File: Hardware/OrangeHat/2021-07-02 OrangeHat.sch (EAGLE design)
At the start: 28 parts, among them CON485A JACK_SMD_3MM5, CON485B JACK_SMD_3MM5, IC485 SN75176

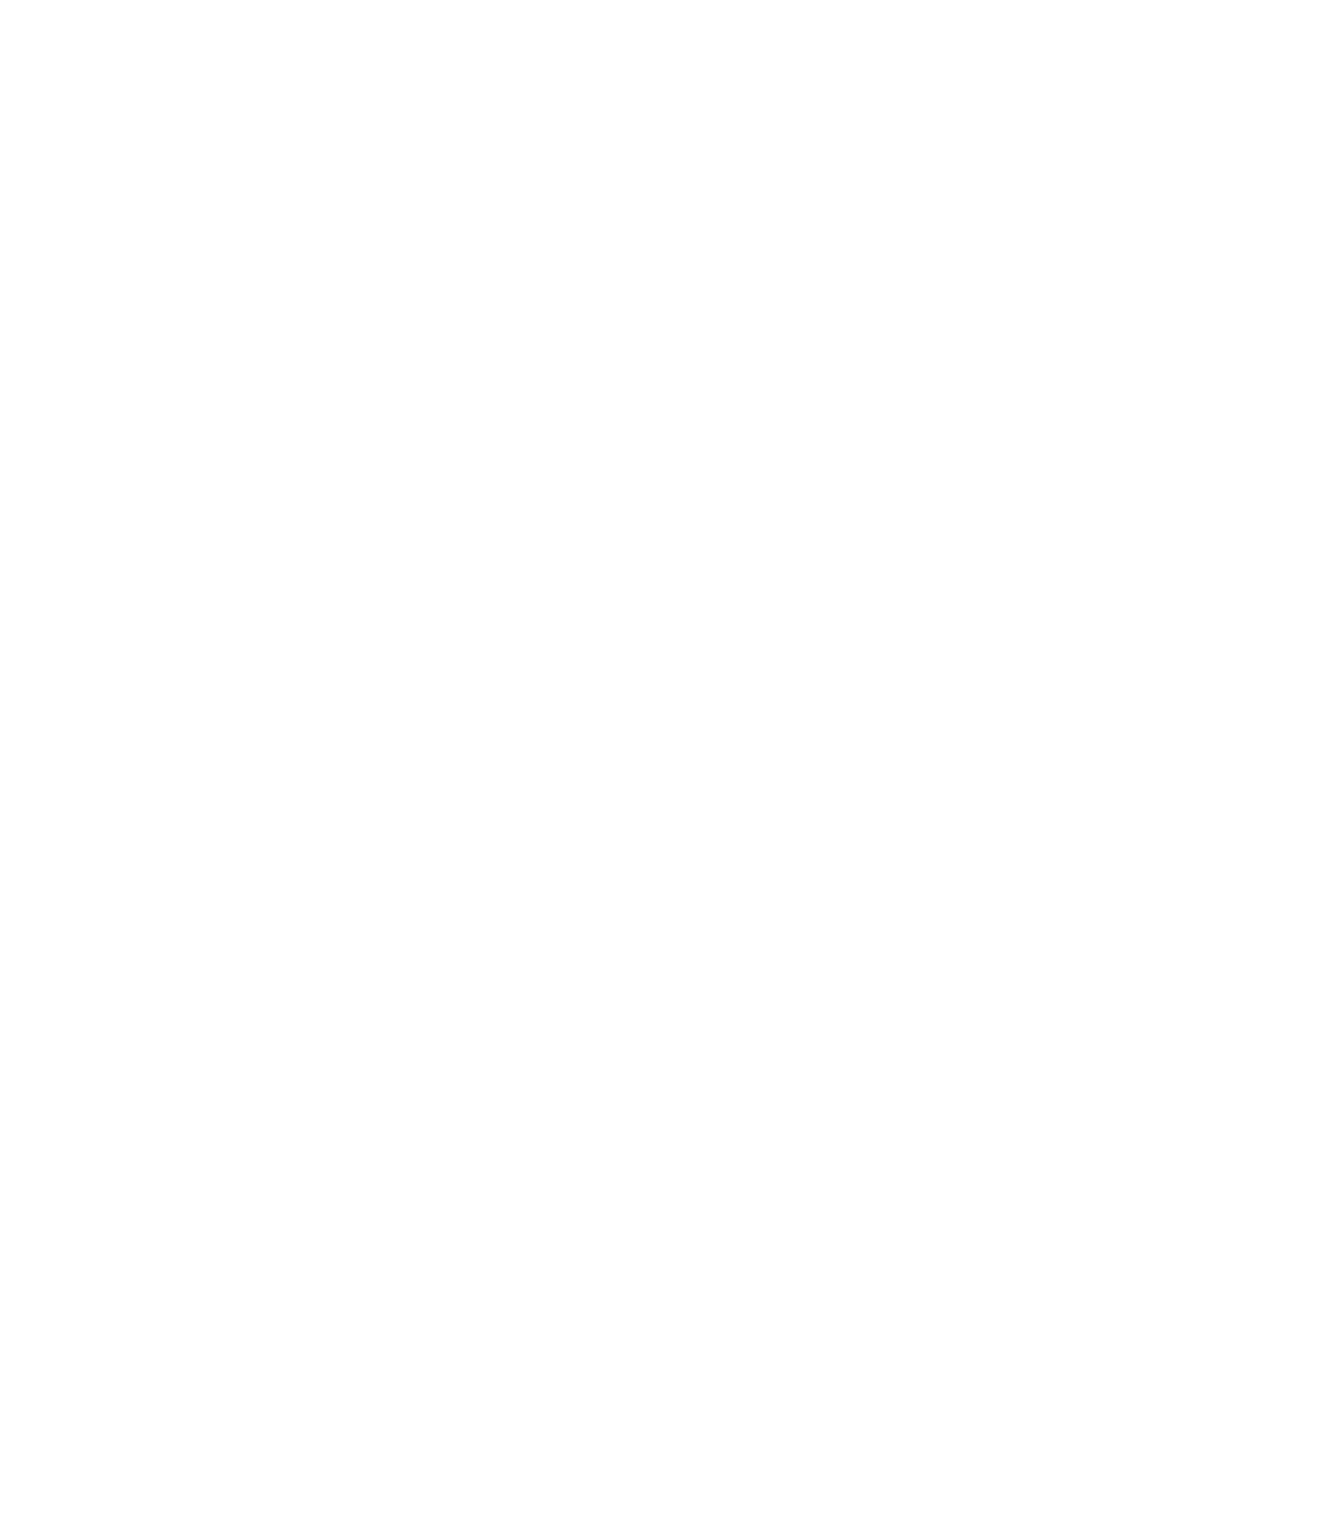
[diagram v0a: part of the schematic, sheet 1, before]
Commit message: Add files via upload
LCD Display Schematics and Initial Placement
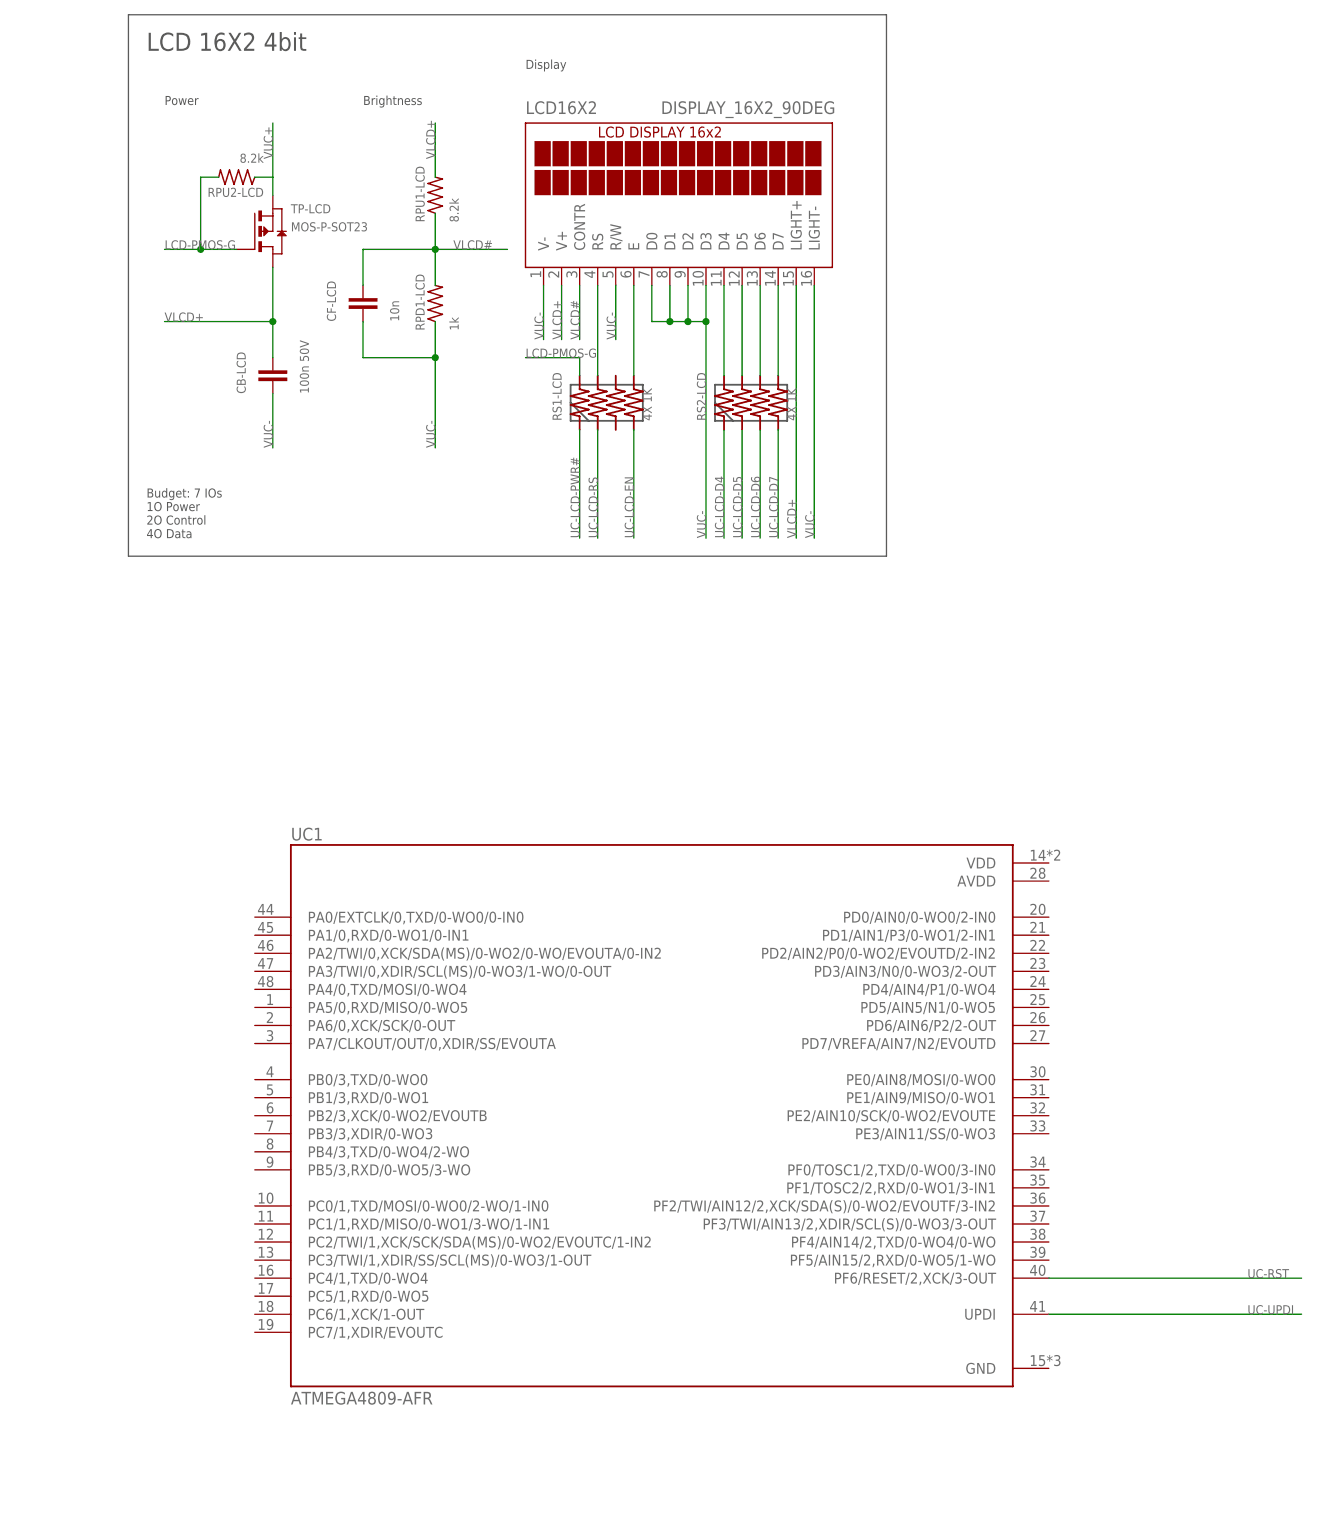
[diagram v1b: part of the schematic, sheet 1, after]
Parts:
- removed DIS1: DISPLAY_16X2_90DEG, 2021-07-02 OrangeHat Library:DISPLAY_16X2_90DEG
- added CB-LCD: 100n 50V, 2021-07-02 OrangeHat Library:C-NPOLC0805
- added CF-LCD: 10n, 2021-07-02 OrangeHat Library:C-NPOLC0805
- added LCD16X2: DISPLAY_16X2_90DEG, 2021-07-02 OrangeHat Library:DISPLAY_16X2_90DEG
- added RPD1-LCD: 1k, 2021-07-02 OrangeHat Library:RM0805
- added RPU1-LCD, RPU2-LCD: 8.2k, 2021-07-02 OrangeHat Library:RM0805
- added RS1-LCD, RS2-LCD: 4X 1K, 2021-07-02 OrangeHat Library:RAC164
- added TP-LCD: MOS-P-SOT23, 2021-07-02 OrangeHat Library:MOS-P-SOT23
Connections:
- removed net N$14: DIS1.LIGHT+
- removed net N$15: DIS1.LIGHT-
- removed net N$3: DIS1.V-
- removed net N$5: DIS1.V+
- removed net N$6: DIS1.CONTR
- removed net N$8: DIS1.R/W
- new net LCD-PMOS-G: RPU2-LCD.2, RS1-LCD.1B, TP-LCD.G
- new net UC-LCD-D4: RS2-LCD.1A
- new net UC-LCD-D5: RS2-LCD.2A
- new net UC-LCD-D6: RS2-LCD.3A
- new net UC-LCD-D7: RS2-LCD.4A
- new net UC-LCD-EN: RS1-LCD.4A
- new net UC-LCD-PWR#: RS1-LCD.1A
- new net UC-LCD-RS: RS1-LCD.2A
- new net VLCD#: CF-LCD.2, LCD16X2.CONTR, RPD1-LCD.2, RPU1-LCD.1
- new net VLCD+: CB-LCD.2, LCD16X2.LIGHT+, LCD16X2.V+, RPU1-LCD.2, TP-LCD.D
- net N$10: now also LCD16X2.D4, RS2-LCD.1B; no longer DIS1.D4
- net N$11: now also LCD16X2.D5, RS2-LCD.2B; no longer DIS1.D5
- net N$12: now also LCD16X2.D6, RS2-LCD.3B; no longer DIS1.D6
- net N$13: now also LCD16X2.D7, RS2-LCD.4B; no longer DIS1.D7
- net N$7: now also LCD16X2.RS, RS1-LCD.2B; no longer DIS1.RS
- net N$9: now also LCD16X2.E, RS1-LCD.4B; no longer DIS1.E
- net VUC+: now also RPU2-LCD.1, TP-LCD.S
- net VUC-: now also CB-LCD.1, CF-LCD.1, LCD16X2.D0, LCD16X2.D1, LCD16X2.D2, LCD16X2.D3, LCD16X2.LIGHT-, LCD16X2.R/W, LCD16X2.V-, RPD1-LCD.1
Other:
- note added: "Brightness"
- note added: "Budget: 7 IOs 1O Power 2O Control 4O Data"
- note added: "Display"
- note added: "LCD 16X2 4bit"
- note added: "Power"

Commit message: Add files via upload
Added Servo schematics and initial placement. Adjusted/created footprints.
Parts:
- removed U$10, U$11, U$4, U$5, U$6, U$7, U$8, U$9: PIWARSRPIHAT_CON3254-MIN, 2021-07-02 OrangeHat Library:PIWARSRPIHAT_CON3254-MIN
- added CB1-SRVO, CB1-SRVO1, CB2-SRVO, CB3-SRVO: 1u, 2021-07-02 OrangeHat Library:C-NPOLC0805
- added CF2-SRVO: 10n, 2021-07-02 OrangeHat Library:C-NPOLC0805
- added CP-SRVO: 100uF 6V3, 2021-07-02 OrangeHat Library:C-POLE2.5-5
- added F-SRVO: PTC-M5040, 2021-07-02 OrangeHat Library:PTC-M5040
- added LF1-SRVO, LF1-SRVO1: BEAD 3A, 2021-07-02 OrangeHat Library:L-M2016
- added RD2-SRVO: 1k, 2021-07-02 OrangeHat Library:RM0805
- added RS1-SRVO, RS2-SRVO: 4X 1K, 2021-07-02 OrangeHat Library:RAC164
- added RS3-SRVO: 1K, 2021-07-02 OrangeHat Library:RM0805
- added RU1-SRVO: 100k, 2021-07-02 OrangeHat Library:RM0805
- added RU2-SRVO: 8.2k, 2021-07-02 OrangeHat Library:RM0805
- added TP-SRVO: MOS-P-TO252, 2021-07-02 OrangeHat Library:MOS-P-TO252
- added U$1: SERVO8, 2021-07-02 OrangeHat Library:SERVO8
- added U$3: ACS712, 2021-07-02 OrangeHat Library:ACS712
- renumbered RPD1-LCD to RD1-LCD, RPU1-LCD to RU1-LCD, RPU2-LCD to RU2-LCD
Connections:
- new net N$15: CB1-SRVO.1, LF1-SRVO1.1
- new net N$21: CB1-SRVO1.2, U$3.FILTER
- new net N$23: RS2-SRVO.1A, U$1.8
- new net N$24: RS2-SRVO.2A, U$1.7
- new net N$25: RS2-SRVO.3A, U$1.6
- new net N$26: RS2-SRVO.4A, U$1.5
- new net N$27: RS1-SRVO.1A, U$1.4
- new net N$28: RS1-SRVO.2A, U$1.3
- new net N$29: RS1-SRVO.3A, U$1.2
- new net N$3: F-SRVO.1
- new net N$30: RS1-SRVO.4A, U$1.1
- new net N$5: RS3-SRVO.2, RU1-SRVO.2, TP-SRVO.G
- new net N$6: F-SRVO.2, RU1-SRVO.1, TP-SRVO.S
- new net UC-ISRVO: U$3.SENSE
- new net UC-SRVO-PWR#: RS3-SRVO.1
- new net UC-SRVO1: RS1-SRVO.4B
- new net UC-SRVO2: RS1-SRVO.3B
- new net UC-SRVO3: RS1-SRVO.2B
- new net UC-SRVO4: RS1-SRVO.1B
- new net UC-SRVO5: RS2-SRVO.4B
- new net UC-SRVO6: RS2-SRVO.3B
- new net UC-SRVO7: RS2-SRVO.2B
- new net UC-SRVO8: RS2-SRVO.1B
- new net UC-VSRVO: CF2-SRVO.2, RD2-SRVO.2, RU2-SRVO.1
- new net VSRVO#A: RU2-SRVO.2, TP-SRVO.D, U$3.IIN
- new net VSRVO#B: CB1-SRVO.2, LF1-SRVO.1, U$3.IOUT
- new net VSRVO+: CB2-SRVO.2, CB3-SRVO.2, CP-SRVO.+, LF1-SRVO.2, U$1.+
- new net VSRVO-: CB2-SRVO.1, CB3-SRVO.1, CP-SRVO.-, LF1-SRVO1.2, U$1.-
- net VUC+: now also U$3.+
- net VUC-: now also CB1-SRVO1.1, CF2-SRVO.1, RD2-SRVO.1, U$3.-
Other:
- note added: "BUDGET: 11 IOs 1O Power 8O PPM 50Hz 2I ADC"
- note added: "BUDGET: 3 IOs 1O Control 2X UART"
- note added: "BUDGET: 7 IOs 1O Power 2O Control 4O Data"
- note added: "Current Sense"
- note added: "Filters"
- note added: "IDEAS: UC+PMOS power control"
- note added: "Power Switch"
- note added: "SERVO"
- note added: "Servo Connectors"
- note added: "Voltage Sense"
- note removed: "Budget: 7 IOs 1O Power 2O Control 4O Data"
- moved on the sheet: LCD16X2, RS1-LCD, RS2-LCD

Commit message: Add files via upload
Adds LED for servo power
Tidy up packages and keepouts
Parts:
- removed CB485: 100n 50V, 2021-07-02 OrangeHat Library:C-NPOLC0805
- removed CF485: 100n 50v, 2021-07-02 OrangeHat Library:C-NPOLC0805
- removed CON485A, CON485B: JACK_SMD_3MM5, 2021-07-02 OrangeHat Library:JACK_SMD_3MM5
- removed CP485: 100uF 6V3, 2021-07-02 OrangeHat Library:C-POLE2.5-5
- removed IC485: SN75176, 2021-07-02 OrangeHat Library:RS485
- removed LF485A, LF485B: BEAD 500mA, 2021-07-02 OrangeHat Library:L-0805
- removed RPD485, RPU485: 720, 2021-07-02 OrangeHat Library:RM0805
- removed RS458A: 4X 1K, 2021-07-02 OrangeHat Library:RAC164
- removed RS485B, RS485C: 10, 2021-07-02 OrangeHat Library:RR0805
- removed RT485: 120, 2021-07-02 OrangeHat Library:RM0805
- added CB-485: 100n 50V, 2021-07-02 OrangeHat Library:C-NPOL
- added CF-485: 100n 50v, 2021-07-02 OrangeHat Library:C-NPOL
- added CON1-485, CON2-485: JACK_SMD_3MM5, 2021-07-02 OrangeHat Library:JACK_SMD_3MM5
- added CP-485: 100uF 6V3, 2021-07-02 OrangeHat Library:C-POLE2.5-5
- added DL-SRVO: LED, 2021-07-02 OrangeHat Library:LED
- added IC-485: SN75176, 2021-07-02 OrangeHat Library:RS485
- added LF1-485, LF2-485: BEAD 500mA, 2021-07-02 OrangeHat Library:L-M2012
- added RD-485, RU-485: 720, 2021-07-02 OrangeHat Library:R-M2012
- added RD-SRVO: 1K, 2021-07-02 OrangeHat Library:R-M2012
- added RS1-458: 4X 1K, 2021-07-02 OrangeHat Library:RAC164
- added RS2-485, RS3-485: 10, 2021-07-02 OrangeHat Library:R-M2012
- added RT-485: 120, 2021-07-02 OrangeHat Library:R-M2012
- CB-LCD, CB1-SRVO, CB1-SRVO1, CB2-SRVO, CB3-SRVO, CF-LCD, CF2-SRVO: device 2021-07-02 OrangeHat Library:C-NPOLC0805 -> 2021-07-02 OrangeHat Library:C-NPOL
- RD1-LCD, RD2-SRVO, RS3-SRVO, RU1-LCD, RU1-SRVO, RU2-LCD, RU2-SRVO: device 2021-07-02 OrangeHat Library:RM0805 -> 2021-07-02 OrangeHat Library:R-M2012
- renumbered U$3 to IC-SRVO
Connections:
- new net N$22: DL-SRVO.+, RD-SRVO.2
- net CHA485: now also CON1-485.L, CON1-485.LX, CON2-485.L, CON2-485.LX, IC-485.A, RD-485.2, RT-485.1; no longer CON485A.L, CON485A.LX, CON485B.L, CON485B.LX, IC485.A, RPD485.2, RT485.1
- net CHB485: now also CON1-485.R, CON1-485.RX, CON2-485.R, CON2-485.RX, IC-485.B, RT-485.2, RU-485.1; no longer CON485A.R, CON485A.RX, CON485B.R, CON485B.RX, IC485.B, RPU485.1, RT485.2
- net N$1: now also IC-485.RXO, RS1-458.1B; no longer IC485.RXO, RS458A.1B
- net N$16: now also IC-485.TXI, RS1-458.4B; no longer IC485.TXI, RS458A.4B
- net N$17: now also CON1-485.SHIELD, RS2-485.2; no longer CON485A.SHIELD, RS485B.2
- net N$18: now also CON2-485.SHIELD, RS3-485.2; no longer CON485B.SHIELD, RS485C.2
- net N$19: now also CF-485.1, LF2-485.1; no longer CF485.1, LF485B.1
- net N$2: now also IC-485.RXEN#, RS1-458.2B; no longer IC485.RXEN#, RS458A.2B
- net N$20: now also CF-485.2, LF1-485.1; no longer CF485.2, LF485A.1
- net N$4: now also IC-485.TXEN, RS1-458.3B; no longer IC485.TXEN, RS458A.3B
- net UC_RXI485: now also RS1-458.1A; no longer RS458A.1A
- net UC_TXEN485: now also RS1-458.3A; no longer RS458A.3A
- net UC_TXO485: now also RS1-458.4A; no longer RS458A.4A
- net V+485: now also CB-485.2, CP-485.+, IC-485.V+, LF1-485.2, RU-485.2; no longer CB485.2, CP485.+, IC485.V+, LF485A.2, RPU485.2
- net V-485: now also CB-485.1, CP-485.-, IC-485.V-, LF2-485.2, RD-485.1, RS1-458.2A, RS2-485.1, RS3-485.1; no longer CB485.1, CP485.-, IC485.V-, LF485B.2, RPD485.1, RS458A.2A, RS485B.1, RS485C.1
- net VSRVO+: now also RD-SRVO.1
- net VSRVO-: now also DL-SRVO.-
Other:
- note added: "LED"

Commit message: Assigns microcontroller pins. Draws power planes.
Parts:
- removed CB-485: 100n 50V, 2021-07-02 OrangeHat Library:C-NPOL
- removed CF-485: 100n 50v, 2021-07-02 OrangeHat Library:C-NPOL
- removed CON1-485, CON2-485: JACK_SMD_3MM5, 2021-07-02 OrangeHat Library:JACK_SMD_3MM5
- removed CP-485: 100uF 6V3, 2021-07-02 OrangeHat Library:C-POLE2.5-5
- removed IC-485: SN75176, 2021-07-02 OrangeHat Library:RS485
- removed LF1-485, LF2-485: BEAD 500mA, 2021-07-02 OrangeHat Library:L-M2012
- removed RS1-458: 4X 1K, 2021-07-02 OrangeHat Library:RAC164
- removed U$2: 2020-03-18-BUCK, 2021-07-02 OrangeHat Library:2020-03-18-BUCK
- removed UC1: ATMEGA4809-AFR, 2021-07-02 OrangeHat Library:ATMEGA4809-AFR
- added CB-UC-1, CB-UC-2, CB-UC-3, CB-UC-4, CB1-485: 100n 50V, 2021-07-02 OrangeHat Library:C-NPOL
- added CF1-485: 100n 50v, 2021-07-02 OrangeHat Library:C-NPOL
- added CON1-1, CON2-1: JACK_SMD_3MM5, 2021-07-02 OrangeHat Library:JACK_SMD_3MM5
- added CP1-485: 100uF 6V3, 2021-07-02 OrangeHat Library:C-POLE2.5-5
- added IC-UC-1: ATMEGA4809-AFR, 2021-07-02 OrangeHat Library:ATMEGA4809-AFR
- added IC1-485: SN75176, 2021-07-02 OrangeHat Library:RS485
- added LF-UC-1, LF1-1, LF2-1: BEAD 500mA, 2021-07-02 OrangeHat Library:L-M2012
- added MOD-BUCK: 2020-03-18-BUCK, 2021-07-02 OrangeHat Library:2020-03-18-BUCK
- added RD-UC-1, RU-UC-1: 100k, 2021-07-02 OrangeHat Library:R-M2012
- added RS-RPI-1, RS1-485: 4X 1K, 2021-07-02 OrangeHat Library:RAC164
- added TN-UC-1: MOS-N-SOT23, 2021-07-02 OrangeHat Library:MOS-N-SOT23
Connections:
- removed net IMU-SCL: IMU1.I2C-SDL
- removed net IMU-SDA: IMU1.I2C-SDA
- removed net N$1: IC-485.RXO, RS1-458.1B
- removed net N$16: IC-485.TXI, RS1-458.4B
- removed net N$18: CON2-485.SHIELD, RS3-485.2
- removed net N$2: IC-485.RXEN#, RS1-458.2B
- removed net N$4: IC-485.TXEN, RS1-458.3B
- removed net RPI-COM: CON-RPI.GND_1, CON-RPI.GND_2
- removed net RPI-VCC: CON-RPI.5V_1, CON-RPI.5V_2
- removed net UC_RXI485: RS1-458.1A
- removed net UC_TXEN485: RS1-458.3A
- removed net UC_TXO485: RS1-458.4A
- new net N$14: IC-UC-1.PF4/AIN14/2,TXD/0-WO4/0-WO
- new net N$42: IC-UC-1.PD6/AIN6/P2/2-OUT
- new net N$43: IC-UC-1.PD5/AIN5/N1/0-WO5
- new net N$44: IC1-485.TXEN, RS1-485.3B
- new net N$45: IC1-485.TXI, RS1-485.4B
- new net N$46: CON1-1.SHIELD, RS2-485.2
- new net N$47: CON2-1.SHIELD, RS3-485.2
- new net N$49: IC-UC-1.PC7/1,XDIR/EVOUTC
- new net N$50: IC-UC-1.PC6/1,XCK/1-OUT
- new net N$51: IC-UC-1.PC5/1,RXD/0-WO5
- new net N$52: IC-UC-1.PC4/1,TXD/0-WO4
- new net N$53: RS-RPI-1.4B
- new net N$62: IC-UC-1.PA6/0,XCK/SCK/0-OUT
- new net N$8: IC-UC-1.PF5/AIN15/2,RXD/0-WO5/1-WO
- new net UC-485-RXEN#: IC-UC-1.PC3/TWI/1,XDIR/SS/SCL(MS)/0-WO3/1-OUT, RS1-485.2A
- new net UC-485-RXI: IC-UC-1.PC1/1,RXD/MISO/0-WO1/3-WO/1-IN1, RS1-485.1A
- new net UC-485-TXEN: IC-UC-1.PC2/TWI/1,XCK/SCK/SDA(MS)/0-WO2/EVOUTC/1-IN2, RS1-485.3A
- new net UC-485-TXO: IC-UC-1.PC0/1,TXD/MOSI/0-WO0/2-WO/1-IN0, RS1-485.4A
- new net UC-IMU-FSYNC: IC-UC-1.PA5/0,RXD/MISO/0-WO5, IMU1.FSYNC
- new net UC-IMU-INT: IC-UC-1.PA4/0,TXD/MOSI/0-WO4, IMU1.INT
- new net UC-IMU-SCL: IC-UC-1.PA3/TWI/0,XDIR/SCL(MS)/0-WO3/1-WO/0-OUT, IMU1.I2C-SDL
- new net UC-IMU-SDA: IC-UC-1.PA2/TWI/0,XCK/SDA(MS)/0-WO2/0-WO/EVOUTA/0-IN2, IMU1.I2C-SDA
- new net UC-IRPI: IC-UC-1.PD2/AIN2/P0/0-WO2/EVOUTD/2-IN2
- new net UC-RPI-RXI: IC-UC-1.PA1/0,RXD/0-WO1/0-IN1, RS-RPI-1.2B
- new net UC-RPI-TXO: IC-UC-1.PA0/EXTCLK/0,TXD/0-WO0/0-IN0, RS-RPI-1.1B
- new net UC-RST#: IC-UC-1.PF6/RESET/2,XCK/3-OUT, RU-UC-1.1, TN-UC-1.D
- new net UC-VIN: IC-UC-1.PD0/AIN0/0-WO0/2-IN0
- new net UC-VRPI: IC-UC-1.PD1/AIN1/P3/0-WO1/2-IN1
- new net VADC+: CB-UC-4.2, IC-UC-1.AVDD, LF-UC-1.2
- new net VRPI+: CON-RPI.5V_1, CON-RPI.5V_2, MOD-BUCK.V5.2A3.0+
- new net VRPI-: CON-RPI.GND_1, CON-RPI.GND_2, MOD-BUCK.V5.2A3.0-
- net CHA485: now also CON1-1.L, CON1-1.LX, CON2-1.L, CON2-1.LX, IC1-485.A; no longer CON1-485.L, CON1-485.LX, CON2-485.L, CON2-485.LX, IC-485.A
- net CHB485: now also CON1-1.R, CON1-1.RX, CON2-1.R, CON2-1.RX, IC1-485.B; no longer CON1-485.R, CON1-485.RX, CON2-485.R, CON2-485.RX, IC-485.B
- net N$17: now also RS-RPI-1.4A; no longer CON1-485.SHIELD, RS2-485.2
- net N$19: now also CF1-485.1, IC1-485.RXO, LF2-1.1, RS1-485.1B; no longer CF-485.1, LF2-485.1
- net N$20: now also CF1-485.2, IC1-485.RXEN#, LF1-1.1, RS1-485.2B; no longer CF-485.2, LF1-485.1
- net RPI-RST: now also RS-RPI-1.3A
- net RPI-RXI: now also RS-RPI-1.1A
- net RPI-TXO: now also RS-RPI-1.2A
- net UC-ISRVO: now also IC-UC-1.PD4/AIN4/P1/0-WO4
- net UC-LCD-D4: now also IC-UC-1.PB0/3,TXD/0-WO0
- net UC-LCD-D5: now also IC-UC-1.PB1/3,RXD/0-WO1
- net UC-LCD-D6: now also IC-UC-1.PB2/3,XCK/0-WO2/EVOUTB
- net UC-LCD-D7: now also IC-UC-1.PB3/3,XDIR/0-WO3
- net UC-LCD-EN: now also IC-UC-1.PB4/3,TXD/0-WO4/2-WO
- net UC-LCD-PWR#: now also IC-UC-1.PA7/CLKOUT/OUT/0,XDIR/SS/EVOUTA
- net UC-LCD-RS: now also IC-UC-1.PB5/3,RXD/0-WO5/3-WO
- net UC-RST: now also RD-UC-1.2, RS-RPI-1.3B, TN-UC-1.G; no longer UC1.PF6/RESET/2,XCK/3-OUT
- net UC-SRVO-PWR#: now also IC-UC-1.PD7/VREFA/AIN7/N2/EVOUTD
- net UC-SRVO1: now also IC-UC-1.PE0/AIN8/MOSI/0-WO0
- net UC-SRVO2: now also IC-UC-1.PE1/AIN9/MISO/0-WO1
- net UC-SRVO3: now also IC-UC-1.PE2/AIN10/SCK/0-WO2/EVOUTE
- net UC-SRVO4: now also IC-UC-1.PE3/AIN11/SS/0-WO3
- net UC-SRVO5: now also IC-UC-1.PF0/TOSC1/2,TXD/0-WO0/3-IN0
- net UC-SRVO6: now also IC-UC-1.PF1/TOSC2/2,RXD/0-WO1/3-IN1
- net UC-SRVO7: now also IC-UC-1.PF2/TWI/AIN12/2,XCK/SDA(S)/0-WO2/EVOUTF/3-IN2
- net UC-SRVO8: now also IC-UC-1.PF3/TWI/AIN13/2,XDIR/SCL(S)/0-WO3/3-OUT
- net UC-UPDI: now also IC-UC-1.UPDI; no longer UC1.UPDI
- net UC-VSRVO: now also IC-UC-1.PD3/AIN3/N0/0-WO3/2-OUT
- net V+485: now also CB1-485.2, CP1-485.+, IC1-485.V+, LF1-1.2; no longer CB-485.2, CP-485.+, IC-485.V+, LF1-485.2
- net V-485: now also CB1-485.1, CP1-485.-, IC1-485.V-, LF2-1.2; no longer CB-485.1, CP-485.-, IC-485.V-, LF2-485.2, RS1-458.2A
- net VIN+: now also MOD-BUCK.VIN+
- net VIN-: now also MOD-BUCK.VIN-
- net VSRVO+: now also MOD-BUCK.V5.8A3.0+
- net VSRVO-: now also MOD-BUCK.V5.8A3.0-
- net VUC+: now also CB-UC-1.2, CB-UC-2.2, CB-UC-3.2, IC-UC-1.VDD, LF-UC-1.1, MOD-BUCK.V5.0A1.0+, RU-UC-1.2
- net VUC-: now also CB-UC-1.1, CB-UC-2.1, CB-UC-3.1, CB-UC-4.1, IC-UC-1.GND, MOD-BUCK.V5.0A1.0-, RD-UC-1.1, TN-UC-1.S
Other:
- note added: "BUCK MODULE"
- note added: "MICROCONTROLLER"
- note added: "RPI"
- note added: "Reset"
